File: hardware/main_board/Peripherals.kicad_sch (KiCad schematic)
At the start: 0 parts

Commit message: drew schematic
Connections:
- no-connect marks 0 -> 1
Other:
- sheet Periph Board 1 renamed Periph Int 1
- sheet Periph Board 2 renamed Periph Int 2
- sheet Periph Board 3 renamed Periph Int 3
- sheet Periph Board 4 renamed Periph Int 4
- sheet Periph Board 5 renamed Periph Int 5
- note added: "Each PBoard: 38.425 mA @ 3V3 11.2 mA @ 5V x5 -> 192.125 mA @ 3V3 x5 -> 55.2 @ 5V"
- note added: "Hierarchical Labels"
- note removed: "SPI0"
- note removed: "SPI1"

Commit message: save before nuke SPI ADC
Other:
- removed sheet Periph Int 5
- added sheet Periph Int 0 (P_BOARD_INT.kicad_sch)

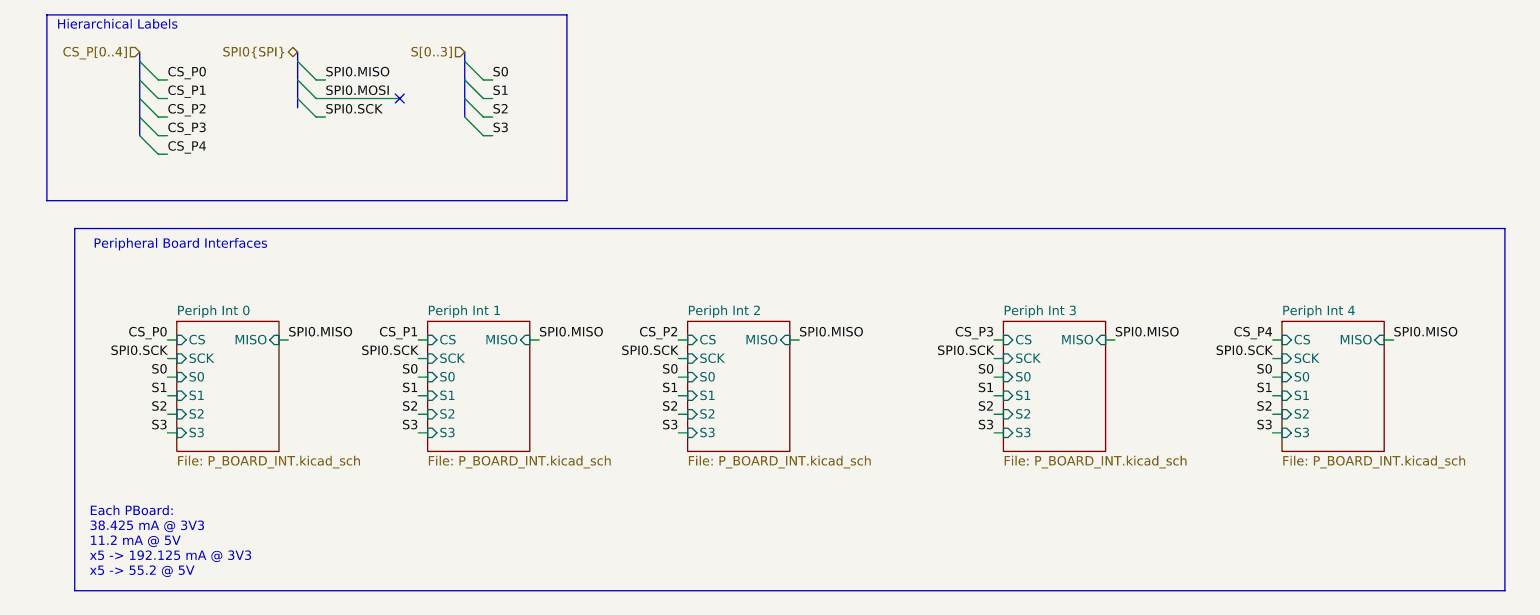
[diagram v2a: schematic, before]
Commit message: port to i2c for both boards. periph board passes drc
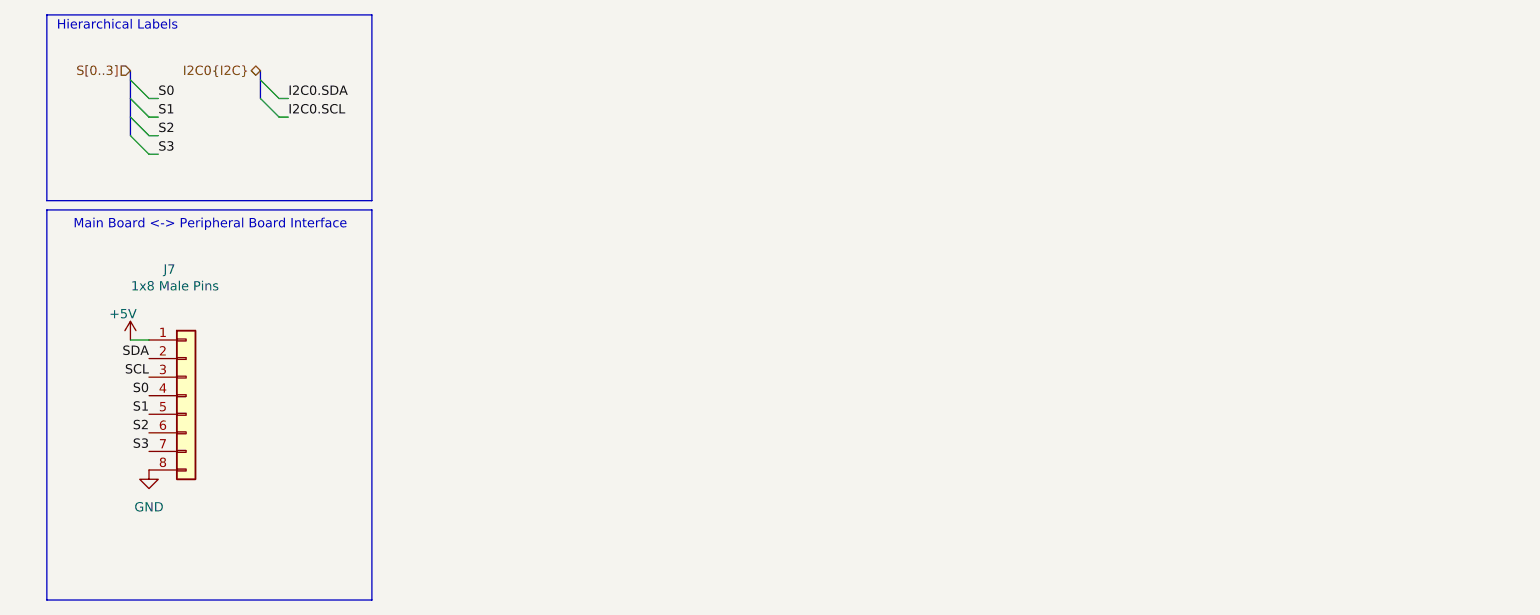
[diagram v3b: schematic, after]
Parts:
- added J7: 1x8 Male Pins, Connector_PinSocket_2.54mm:PinSocket_1x08_P2.54mm_Vertical, symbol Connector_Generic:Conn_01x08
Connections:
- net S0: now also J7.4 (Pin_4)
- net S1: now also J7.5 (Pin_5)
- net S2: now also J7.6 (Pin_6)
- net S3: now also J7.7 (Pin_7)
- new net +5V: J7.1 (Pin_1)
- new net GND: J7.8 (Pin_8)
- new net SCL: J7.3 (Pin_3)
- new net SDA: J7.2 (Pin_2)
- no-connect marks 1 -> 0
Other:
- removed sheet Periph Int 0
- removed sheet Periph Int 1
- removed sheet Periph Int 2
- removed sheet Periph Int 3
- removed sheet Periph Int 4
- note added: "Main Board <-> Peripheral Board Interface"
- note removed: "Each PBoard: 38.425 mA @ 3V3 11.2 mA @ 5V x5 -> 192.125 mA @ 3V3 x5 -> 55.2 @ 5V"
- note removed: "Peripheral Board Interfaces"
